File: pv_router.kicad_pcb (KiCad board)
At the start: 4 copper layers, 70 x 70 mm, 83 parts, among them IC1 AP63203WU-7, IC2 ATM90E26-YU-B, J1 Barrel_Jack_Switch_Pin3Ring, J10 Conn_01x03_Pin, J2 AudioJack3, J3 AudioJack3, J4 Barrel_Jack_Switch_Pin3Ring, J5 UART, J6 ToSSR, J7 USB_A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

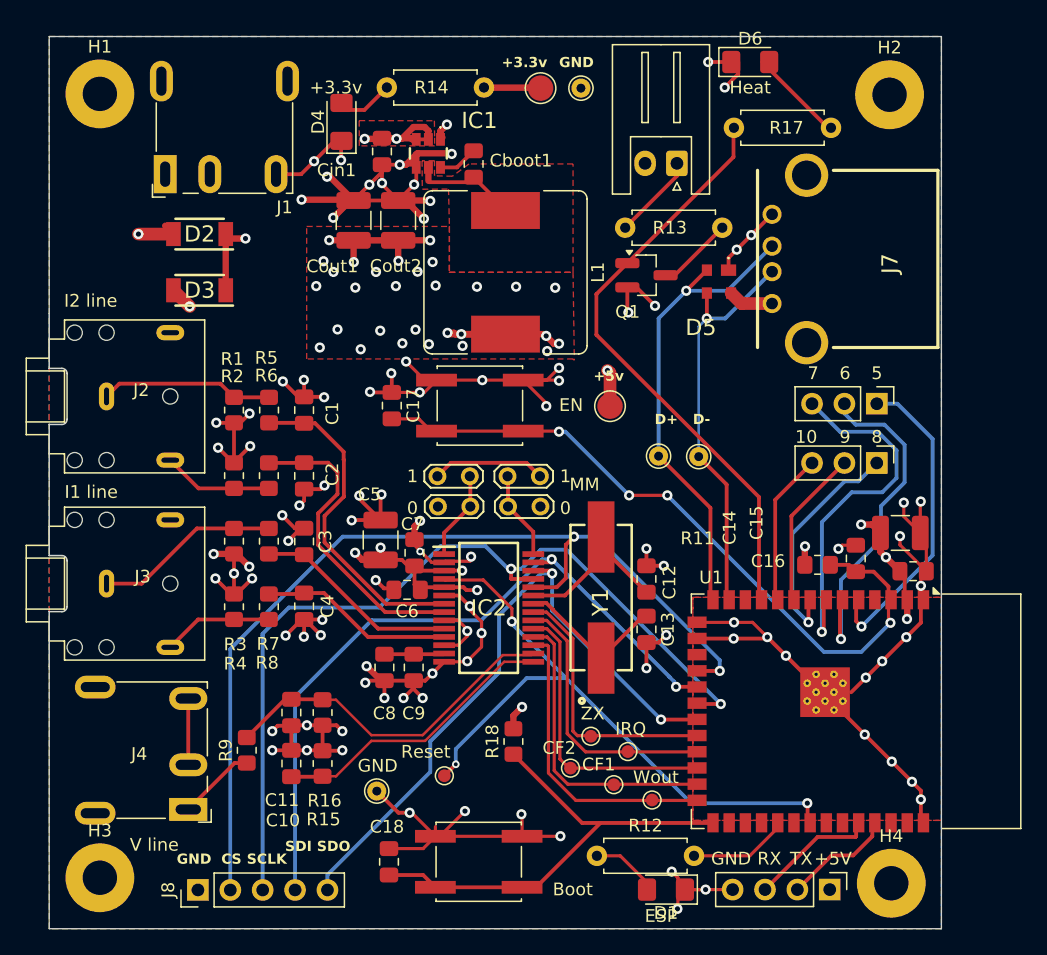
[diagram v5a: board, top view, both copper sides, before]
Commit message: fix: add some GND vias
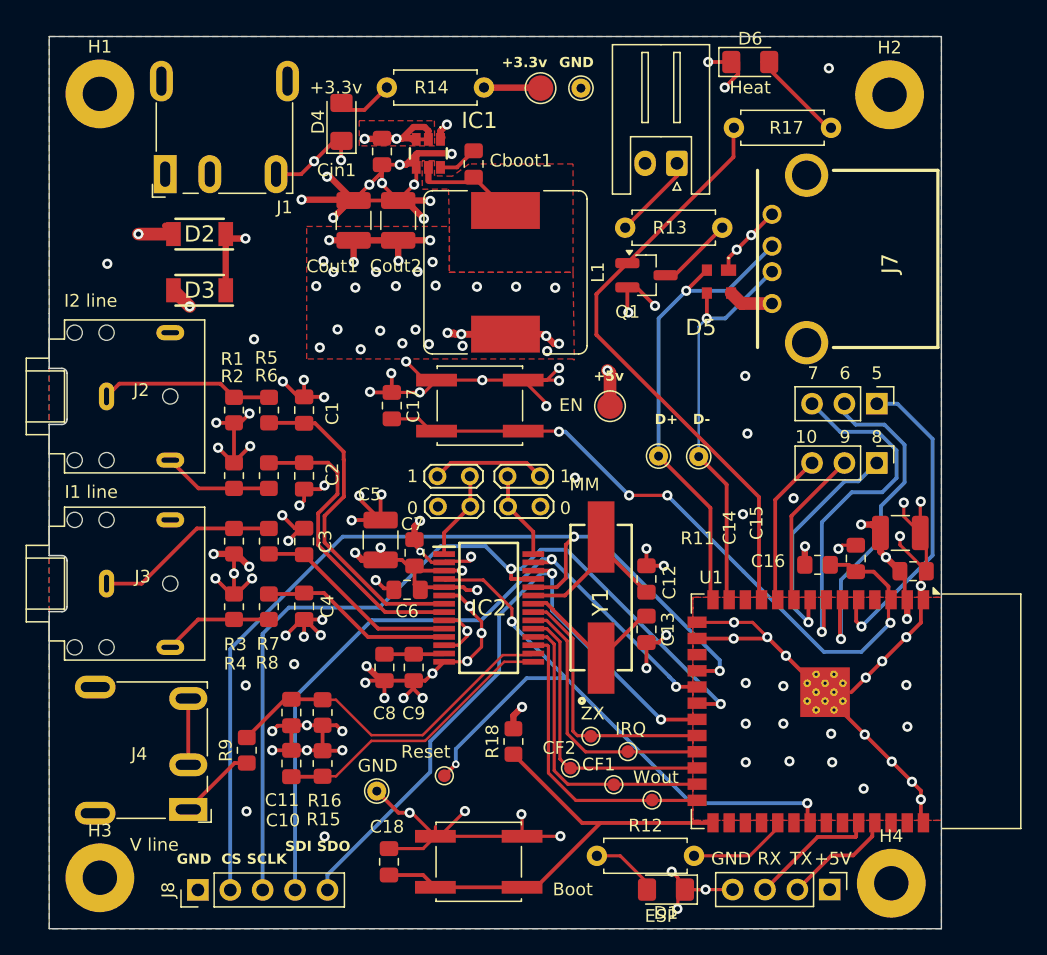
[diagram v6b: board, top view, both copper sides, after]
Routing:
- net GND: vias 96 -> 119
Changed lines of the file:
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@@
 	)
 	(via
+		(at 140.42 130.91)
+		(size 0.8)
+		(drill 0.4)
+		(layers "F.Cu" "B.Cu")
+		(free yes)
+		(net 1)
+	)
+	(via
 		(at 147.285 94.215)
 		(size 0.8)
@@
 	)
 	(via
+		(at 144.22 129.24)
+		(size 0.8)
+		(drill 0.4)
+		(layers "F.Cu" "B.Cu")
+		(free yes)
+		(net 1)
+	)
+	(via
 		(at 165 107)
 		(size 0.8)
@@
 	)
 	(via
+		(at 186.43 136.94)
+		(size 0.8)
+		(drill 0.4)
+		(layers "F.Cu" "B.Cu")
+		(free yes)
+		(net 1)
+	)
+	(via
 		(at 142.5 136)
 		(size 0.8)
@@
 	)
 	(via
+		(at 182.6 133.91)
+		(size 0.8)
+		(drill 0.4)
+		(layers "F.Cu" "B.Cu")
+		(free yes)
+		(net 1)
+	)
+	(via
 		(at 171.86 129.56)
 		(size 0.8)
@@
 	)
 	(via
+		(at 192.33 134.15)
+		(size 0.8)
+		(drill 0.4)
+		(layers "F.Cu" "B.Cu")
+		(free yes)
+		(net 1)
+	)
+	(via
 		(at 158.92 126.81)
 		(size 0.8)
@@
 	)
 	(via
+		(at 146.61 142.76)
+		(size 0.8)
+		(drill 0.4)
+		(layers "F.Cu" "B.Cu")
+		(free yes)
+		(net 1)
+	)
+	(via
 		(at 150.620334 122.649666)
 		(size 0.8)
@@
 	)
 	(via
+		(at 183.08 136.86)
+		(size 0.8)
+		(drill 0.4)
+		(layers "F.Cu" "B.Cu")
+		(free yes)
+		(net 1)
+	)
+	(via
 		(at 170.44 101.65)
 		(size 0.8)
@@
 	)
 	(via
+		(at 188.9 139.01)
+		(size 0.8)
+		(drill 0.4)
+		(layers "F.Cu" "B.Cu")
+		(free yes)
+		(net 1)
+	)
+	(via
 		(at 151.3 131.9)
 		(size 0.8)
@@
 	)
 	(via
+		(at 179.65 136.94)
+		(size 0.8)
+		(drill 0.4)
+		(layers "F.Cu" "B.Cu")
+		(free yes)
+		(net 1)
+	)
+	(via
 		(at 142.5 134.5)
 		(size 0.8)
@@
 	)
 	(via
+		(at 183.4 116.23)
+		(size 0.8)
+		(drill 0.4)
+		(layers "F.Cu" "B.Cu")
+		(free yes)
+		(net 1)
+	)
+	(via
 		(at 151.07 115.93)
 		(size 0.8)
@@
 	)
 	(via
+		(at 179.65 133.91)
+		(size 0.8)
+		(drill 0.4)
+		(layers "F.Cu" "B.Cu")
+		(free yes)
+		(net 1)
+	)
+	(via
 		(at 164 109)
 		(size 0.8)
@@
 	)
 	(via
+		(at 141.07 103.75)
+		(size 0.8)
+		(drill 0.4)
+		(layers "F.Cu" "B.Cu")
+		(free yes)
+		(net 1)
+	)
+	(via
 		(at 165 106)
 		(size 0.8)
@@
 	)
 	(via
+		(at 186.35 134.7)
+		(size 0.8)
+		(drill 0.4)
+		(layers "F.Cu" "B.Cu")
+		(free yes)
+		(net 1)
+	)
+	(via
+		(at 179.43 117.48)
+		(size 0.8)
+		(drill 0.4)
+		(layers "F.Cu" "B.Cu")
+		(free yes)
+		(net 1)
+	)
+	(via
 		(at 172.53 101.13)
 		(size 0.8)
@@
 	)
 	(via
+		(at 129.56 97.83)
+		(size 0.8)
+		(drill 0.4)
+		(layers "F.Cu" "B.Cu")
+		(free yes)
+		(net 1)
+	)
+	(via
 		(at 149.8 130.7)
 		(size 0.8)
@@
 	)
 	(via
+		(at 179.61 106.63)
+		(size 0.8)
+		(drill 0.4)
+		(layers "F.Cu" "B.Cu")
+		(free yes)
+		(net 1)
+	)
+	(via
 		(at 146.8 91)
 		(size 0.8)
@@
 	)
 	(via
+		(at 179.65 130.72)
+		(size 0.8)
+		(drill 0.4)
+		(layers "F.Cu" "B.Cu")
+		(free yes)
+		(net 1)
+	)
+	(via
 		(at 155.07075 129.97075)
 		(size 0.8)
@@
 	)
 	(via
+		(at 140.48 140.79)
+		(size 0.8)
+		(drill 0.4)
+		(layers "F.Cu" "B.Cu")
+		(free yes)
+		(net 1)
+	)
+	(via
 		(at 153.28 140.9)
 		(size 0.8)
@@
 	)
 	(via
+		(at 179.78 111.15)
+		(size 0.8)
+		(drill 0.4)
+		(layers "F.Cu" "B.Cu")
+		(free yes)
+		(net 1)
+	)
+	(via
 		(at 140.72 109.58)
 		(size 0.8)
@@
 	)
 	(via
+		(at 166.25 114.61)
+		(size 0.8)
+		(drill 0.4)
+		(layers "F.Cu" "B.Cu")
+		(free yes)
+		(net 1)
+	)
+	(via
 		(at 143.55 127)
 		(size 0.8)
@@
 	)
 	(via
+		(at 182.6 130.96)
+		(size 0.8)
+		(drill 0.4)
+		(layers "F.Cu" "B.Cu")
+		(free yes)
+		(net 1)
+	)
+	(via
 		(at 145.78375 89.78375)
 		(size 0.8)
@@
 	)
 	(via
+		(at 192.25 130.88)
+		(size 0.8)
+		(drill 0.4)
+		(layers "F.Cu" "B.Cu")
+		(free yes)
+		(net 1)
+	)
+	(via
 		(at 143.76 119.57)
 		(size 0.8)
@@
 	)
 	(via
+		(at 186.17 82.49)
+		(size 0.8)
+		(drill 0.4)
+		(layers "F.Cu" "B.Cu")
+		(free yes)
+		(net 1)
+	)
+	(via
 		(at 146.43 125.76)
 		(size 0.8)
@@
 	(segment
 		(start 173.5 116)
-		(end 185.78 128.28)
+		(end 179.47 121.97)
 		(width 0.3)
 		(layer "B.Cu")
@@
 	)
 	(segment
+		(start 179.47 121.97)
+		(end 185.78 128.28)
+		(width 0.3)
+		(layer "B.Cu")
+		(net 3)
+	)
+	(segment
 		(start 174.18 131.02)
 		(end 175.605 131.02)
@@
 	)
 	(zone
-		(net 3)
-		(net_name "/esp32/EN")
-		(layer "F.Cu")
-		(name "$teardrop_padvia$")
-		(hatch full 0.1)
-		(priority 30221)
-		(attr
-			(teardrop
-				(type padvia)
-			)
-		)
-		(connect_pads yes
-			(clearance 0)
-		)
-		(min_thickness 0.0254)
-		(filled_areas_thickness no)
-		(fill yes
-			(thermal_gap 0.5)
-			(thermal_bridge_width 0.5)
-			(island_removal_mode 1)
-			(island_area_min 10)
-		)
-		(polygon
-			(pts
-				(xy 172.707686 115.875) (xy 172.707686 116.125) (xy 173.421964 116.392314) (xy 173.501 116) (xy 173.421964 115.607686)
-			)
-		)
-	)
-	(zone
 		(net 1)
 		(net_name "GND")
@@
 	)
 	(zone
+		(net 3)
+		(net_name "/esp32/EN")
+		(layer "F.Cu")
+		(name "$teardrop_padvia$")
+		(hatch full 0.1)
+		(priority 30000)
+		(attr
+			(teardrop
+				(type padvia)
+			)
+		)
+		(connect_pads yes
+			(clearance 0)
+		)
+		(min_thickness 0.0254)
+		(filled_areas_thickness no)
+		(fill yes
+			(thermal_gap 0.5)
+			(thermal_bridge_width 0.5)
+			(island_removal_mode 1)
+			(island_area_min 10)
+		)
+		(polygon
+			(pts
+				(xy 172.707686 115.875) (xy 172.707686 116.125) (xy 173.421964 116.392314) (xy 173.501 116) (xy 173.421964 115.607686)
+			)
+		)
+	)
+	(zone
 		(net 1)
 		(net_name "GND")
@@
 	)
 	(zone
-		(net 3)
-		(net_name "/esp32/EN")
+		(net 5)
+		(net_name "/adc/SCLK")
 		(layer "B.Cu")
 		(name "$teardrop_padvia$")
 		(hatch full 0.1)
-		(priority 30028)
+		(priority 30030)
 		(attr
 			(teardrop
@@
 		(polygon
 			(pts
-				(xy 173.954184 116.666316) (xy 174.166316 116.454184) (xy 173.832588 115.777772) (xy 173.499293 115.999293)
-				(xy 173.277772 116.332588)
+				(xy 177.235816 131.703684) (xy 177.023684 131.915816) (xy 177.357412 132.592228) (xy 177.690707 132.370707)
+				(xy 177.912228 132.037412)
 			)
 		)
 	)
 	(zone
-		(net 5)
-		(net_name "/adc/SCLK")
+		(net 3)
+		(net_name "/esp32/EN")
 		(layer "B.Cu")
 		(name "$teardrop_padvia$")
 		(hatch full 0.1)
-		(priority 30030)
+		(priority 30000)
 		(attr
 			(teardrop
@@
 		(polygon
 			(pts
-				(xy 177.235816 131.703684) (xy 177.023684 131.915816) (xy 177.357412 132.592228) (xy 177.690707 132.370707)
-				(xy 177.912228 132.037412)
+				(xy 173.954184 116.666316) (xy 174.166316 116.454184) (xy 173.832588 115.777772) (xy 173.499293 115.999293)
+				(xy 173.277772 116.332588)
 			)
 		)

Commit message: fix: DRC check
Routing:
- net GND: track 288.9 -> 285.3 mm
- net /esp32/EN: track 55.6 -> 55.0 mm
- net Net-(IC1-SW): track 8.34 -> 7.79 mm
